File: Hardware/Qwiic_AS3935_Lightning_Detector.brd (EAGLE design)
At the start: 25.4 x 25.4 mm, 69 parts, among them U1 AS3935

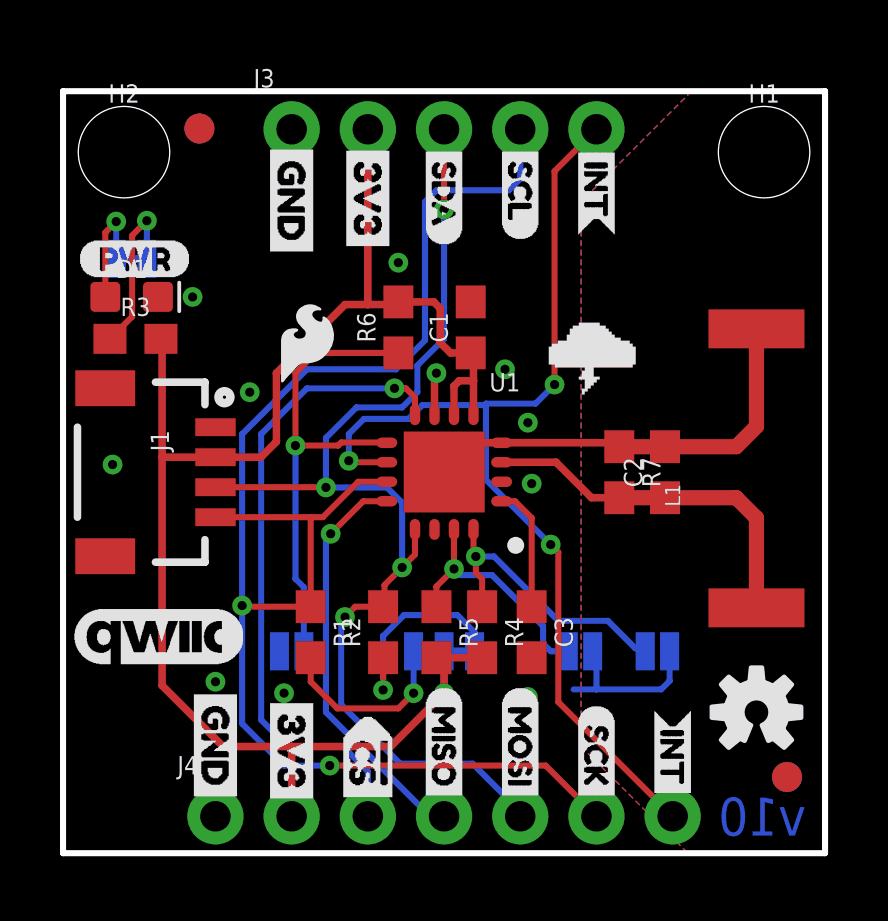
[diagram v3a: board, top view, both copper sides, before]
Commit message: Moves drill hits near standoff, moves LED jumper down, renames IRQ net to INT, and adds info on other address options
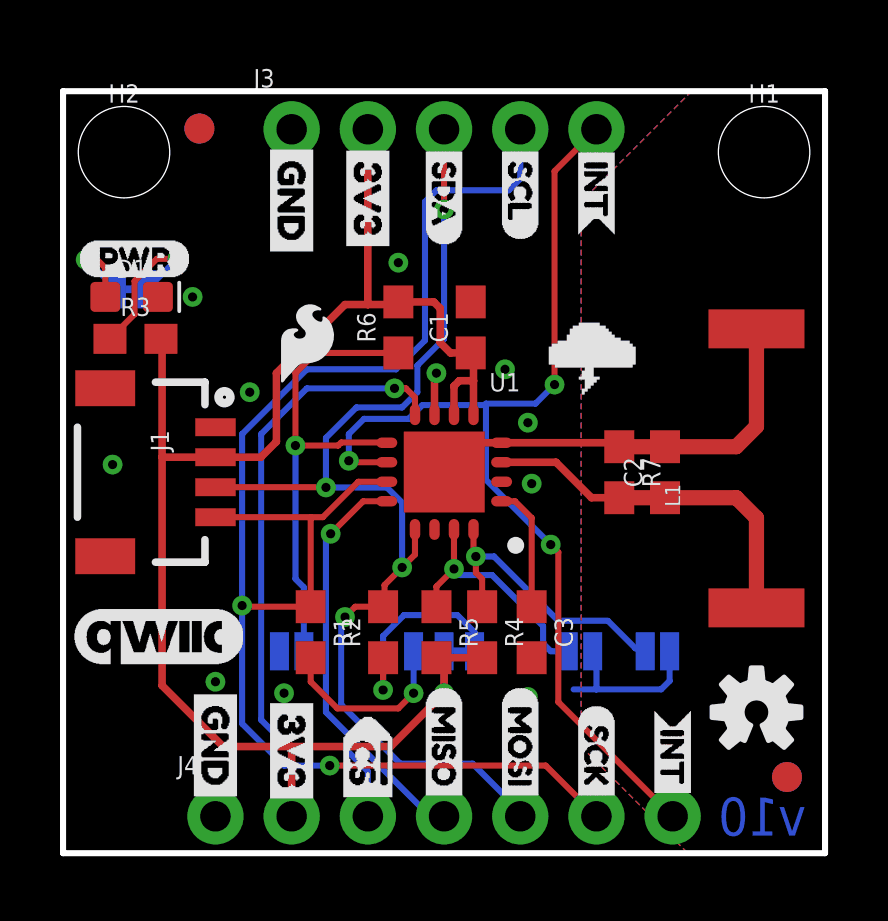
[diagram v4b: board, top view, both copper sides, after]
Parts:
- moved JP5 1.02 mm to (2.29, 18.8)
- moved U$1 1.02 mm to (4.00, 17.0)
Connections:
- net IRQ renamed INT
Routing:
- net N$5: track 3.91 -> 3.17 mm
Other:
- board text added: "Units in Inches"
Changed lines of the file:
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@@
 <setting verticaltext="up"/>
 </settings>
-<grid distance="0.01" unitdist="inch" unit="inch" style="lines" multiple="1" display="yes" altdistance="0.0001" altunitdist="inch" altunit="inch"/>
+<grid distance="0.01" unitdist="inch" unit="inch" style="lines" multiple="1" display="yes" altdistance="0.001" altunitdist="inch" altunit="inch"/>
 <layers>
 <layer number="1" name="Top" color="4" fill="1" visible="yes" active="yes"/>
@@
 <layer number="115" name="ReferenceISLANDS" color="7" fill="1" visible="no" active="no"/>
 <layer number="116" name="Patch_BOT" color="9" fill="4" visible="no" active="no"/>
-<layer number="117" name="PM_Ref" color="26" fill="1" visible="no" active="yes"/>
+<layer number="117" name="PM_Ref" color="26" fill="1" visible="yes" active="yes"/>
 <layer number="118" name="Rect_Pads" color="7" fill="1" visible="no" active="no"/>
-<layer number="119" name="PF_Ref" color="31" fill="1" visible="no" active="yes"/>
-<layer number="120" name="WFL_Ref" color="25" fill="1" visible="no" active="yes"/>
+<layer number="119" name="PF_Ref" color="31" fill="1" visible="yes" active="yes"/>
+<layer number="120" name="WFL_Ref" color="25" fill="1" visible="yes" active="yes"/>
 <layer number="121" name="_tsilk" color="7" fill="1" visible="no" active="no"/>
 <layer number="122" name="_bsilk" color="7" fill="1" visible="no" active="no"/>
@@
 <text x="19.177" y="-19.177" size="1.778" layer="51" font="vector">Elias Santistevan</text>
 <text x="24.765" y="0.5842" size="1.27" layer="16" font="vector" ratio="15" rot="MR0">v10</text>
+<dimension x1="25.4" y1="25.4" x2="0" y2="25.4" x3="12.7" y3="28.194" textsize="1.778" textratio="15" layer="47" dtype="horizontal" unit="inch"/>
+<dimension x1="25.4" y1="0" x2="25.4" y2="25.4" x3="30.226" y3="12.7" textsize="1.778" textratio="15" layer="47" dtype="horizontal" unit="inch"/>
+<text x="4.318" y="-4.572" size="1.778" layer="47" font="vector" ratio="15">Units in Inches</text>
 </plain>
 <attributes>
@@
 <attribute name="VALUE" x="2.032" y="21.717" size="0.6096" layer="27" font="vector" ratio="20" align="top-center"/>
 </element>
-<element name="JP5" library="SparkFun-Jumpers" package="SMT-JUMPER_2_NC_TRACE_SILK" value="LED" x="2.286" y="19.812" smashed="yes" rot="MR180">
-<attribute name="NAME" x="2.286" y="18.669" size="0.6096" layer="26" font="vector" ratio="20" rot="MR180" align="bottom-center"/>
-<attribute name="VALUE" x="2.286" y="20.955" size="0.6096" layer="28" font="vector" ratio="20" rot="MR180" align="top-center"/>
-</element>
-<element name="U$1" library="LED" package="LED0" value="" x="4.003040625" y="17.973040625" smashed="yes" rot="MR0"/>
+<element name="JP5" library="SparkFun-Jumpers" package="SMT-JUMPER_2_NC_TRACE_SILK" value="LED" x="2.286" y="18.796" smashed="yes" rot="MR180">
+<attribute name="NAME" x="2.286" y="17.653" size="0.6096" layer="26" font="vector" ratio="20" rot="MR180" align="bottom-center"/>
+<attribute name="VALUE" x="2.286" y="19.939" size="0.6096" layer="28" font="vector" ratio="20" rot="MR180" align="top-center"/>
+</element>
+<element name="U$1" library="LED" package="LED0" value="" x="4.003040625" y="16.957040625" smashed="yes" rot="MR0"/>
 </elements>
 <signals>
@@
 <wire x1="16.4324" y1="13.0316" x2="14.6186" y2="13.0316" width="0.254" layer="1"/>
 </signal>
-<signal name="IRQ">
+<signal name="INT">
 <contactref element="J4" pad="7"/>
 <contactref element="J3" pad="5"/>
@@
 <wire x1="15.748" y1="14.986" x2="16.383" y2="15.621" width="0.2032" layer="16"/>
 <contactref element="U1" pad="10"/>
-<wire x1="10.7422" y1="13.081" x2="10.7916" y2="13.0316" width="0.2032" layer="1"/>
 <wire x1="9.525" y1="13.081" x2="9.5744" y2="13.0316" width="0.2032" layer="1"/>
 <wire x1="9.5744" y1="13.0316" x2="10.7916" y2="13.0316" width="0.2032" layer="1"/>
@@
 <contactref element="R3" pad="1"/>
 <contactref element="JP5" pad="2"/>
-<wire x1="1.563" y1="17.145" x2="2.30378125" y2="17.88578125" width="0.2032" layer="1"/>
-<wire x1="2.30378125" y1="20.59178125" x2="2.794" y2="21.082" width="0.2032" layer="1"/>
-<via x="2.794" y="21.082" extent="1-16" drill="0.3048"/>
-<wire x1="2.794" y1="21.082" x2="2.794" y2="19.812" width="0.2032" layer="16"/>
-<wire x1="2.30378125" y1="17.88578125" x2="2.30378125" y2="20.59178125" width="0.2032" layer="1"/>
+<via x="3.81" y="19.812" extent="1-16" drill="0.3048"/>
+<wire x1="3.81" y1="19.812" x2="2.794" y2="18.796" width="0.2032" layer="16"/>
+<wire x1="2.3836" y1="19.0698625" x2="3.1257375" y2="19.812" width="0.2032" layer="1"/>
+<wire x1="3.1257375" y1="19.812" x2="3.81" y2="19.812" width="0.2032" layer="1"/>
+<wire x1="1.563" y1="17.145" x2="2.3836" y2="17.9656" width="0.2032" layer="1"/>
+<wire x1="2.3836" y1="17.9656" x2="2.3836" y2="19.0698625" width="0.2032" layer="1"/>
 </signal>
 <signal name="N$5">
 <contactref element="JP5" pad="1"/>
 <contactref element="D1" pad="A"/>
-<wire x1="1.409" y1="18.542" x2="1.409" y2="20.69115" width="0.2032" layer="1"/>
-<wire x1="1.409" y1="20.69115" x2="1.771784375" y2="21.053934375" width="0.2032" layer="1"/>
-<via x="1.771784375" y="21.053934375" extent="1-16" drill="0.3048"/>
-<wire x1="1.771784375" y1="21.053934375" x2="1.771784375" y2="19.818215625" width="0.2032" layer="16"/>
-<wire x1="1.771784375" y1="19.818215625" x2="1.778" y2="19.812" width="0.2032" layer="16"/>
+<wire x1="1.409" y1="18.542" x2="1.409" y2="19.51171875" width="0.2032" layer="1"/>
+<wire x1="1.409" y1="19.51171875" x2="1.136784375" y2="19.783934375" width="0.2032" layer="1"/>
+<wire x1="1.136784375" y1="19.783934375" x2="0.755784375" y2="19.783934375" width="0.2032" layer="1"/>
+<via x="0.755784375" y="19.783934375" extent="1-16" drill="0.3048"/>
+<wire x1="0.755784375" y1="19.783934375" x2="0.790065625" y2="19.783934375" width="0.2032" layer="16"/>
+<wire x1="0.790065625" y1="19.783934375" x2="1.778" y2="18.796" width="0.2032" layer="16"/>
 </signal>
 </signals>

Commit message: Updates lightning detector part to latest - window pane of paste rather than solid block
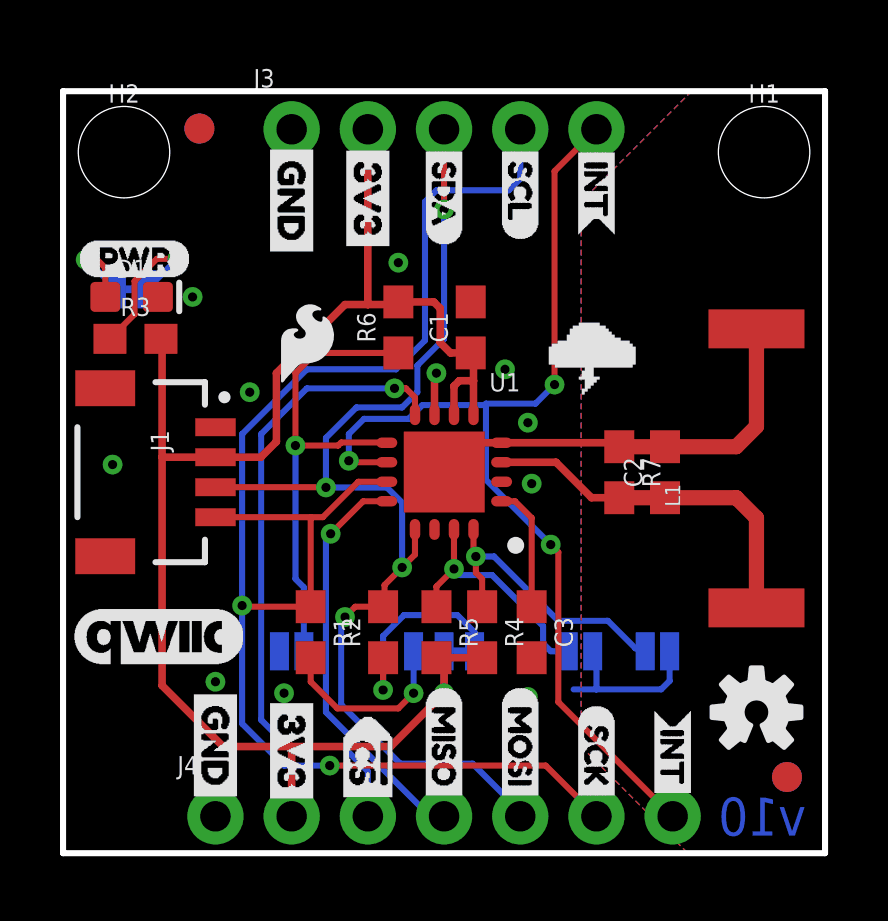
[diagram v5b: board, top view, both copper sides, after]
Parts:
- J1: device SparkFun-Connectors:1X04_1MM_RA -> SparkFun-Connectors:JST04_1MM_RA
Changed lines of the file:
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@@
 <attribute name="REV" value="" x="-7.62" y="-19.05" size="1.778" layer="27" display="off"/>
 </element>
-<element name="J1" library="SparkFun-Connectors" package="1X04_1MM_RA" value="" x="5.08" y="12.7" smashed="yes" rot="R270">
+<element name="J1" library="SparkFun-Connectors" package="JST04_1MM_RA" value="" x="5.08" y="12.7" smashed="yes" rot="R270">
 <attribute name="NAME" x="2.921" y="14.097" size="0.6096" layer="25" font="vector" ratio="20" rot="R270"/>
 <attribute name="PROD_ID" value="CONN-13694" x="5.08" y="12.7" size="1.778" layer="27" rot="R270" display="off"/>

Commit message: List of changes in description from v10 to v11
* Changes three way pull up jumper to disinclude I2C data line - also changes values to 10k
* Removes seperate I2C header and combines I2C and SPI into one header - prevents extraneous trace length on data lines
* Improves layout for better ground pour
* Moves address jumpers and SPI select jumpers
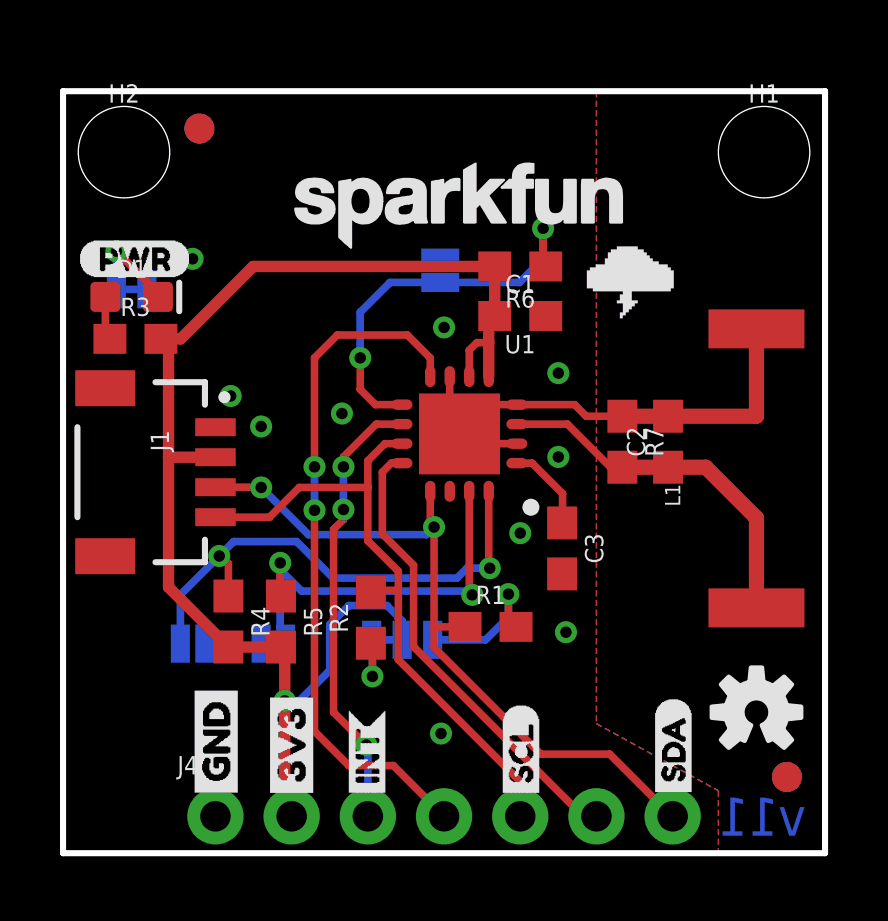
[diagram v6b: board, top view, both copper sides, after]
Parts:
- removed J3: (no value), SparkFun-Connectors:1X05_NO_SILK
- removed LOGO3: SFE_LOGO_FLAME.1_INCH, SparkFun-Aesthetics:SFE_LOGO_FLAME_.1
- removed U$11: (no value), Labels:CS#-<]-04
- removed U$13: (no value), Labels:MISO-(]-03
- removed U$15: (no value), INT_2:INT0
- removed U$16: (no value), Labels:MOSI-(]-03
- removed U$17, U$20: (no value), Labels:3V3-03
- removed U$19: (no value), Labels:SCK-(]-03
- removed U$26: (no value), SDA:SDA0
- removed U$27: (no value), SCL:SCL0
- removed U$29: (no value), INT:INT0
- removed U$38, U$9: (no value), Labels:GND-03
- removed U$4: (no value), Labels:QWIIC_COPYRIGHT_SMALL
- JP4: value JUMPER-SMT_3_2-NC_TRACE_SILK -> JUMPER-SMT_3_1-NC_TRACE_SILK; device SparkFun-Jumpers:SMT-JUMPER_3_2-NC_TRACE_SILK -> SparkFun-Jumpers:SMT-JUMPER_3_1-NC_TRACE_SILK
- R1, R2, R4, R5: value 2.2k -> 10k
- moved U$24 23.4 mm to (10.1, 1.63), turned to 90 degrees
- moved U$25 23.4 mm to (20.3, 1.68), turned to 90 degrees
- moved U$21 22.5 mm to (7.62, 1.55), turned to 90 degrees
- moved U$8 22.4 mm to (5.11, 1.60), turned to 90 degrees
- moved U$28 22.1 mm to (15.3, 1.65), turned to 90 degrees
- moved JP1 15.5 mm to (4.32, 6.99)
- moved U$36 14.4 mm to (3.81, 6.99)
- moved U$35 13.8 mm to (14.4, 21.7)
- moved JP3 13.6 mm to (12.6, 19.4), turned to 90 degrees
- moved U$33 13.0 mm to (7.87, 9.02)
- moved U$37 10.6 mm to (10.2, 6.99)
- moved JP2 10.2 mm to (7.01, 6.99), turned to 0 degrees
- moved R4 8.47 mm to (5.51, 7.72)
- moved R1 6.00 mm to (14.2, 7.54), turned to 0 degrees
- moved R5 5.19 mm to (7.26, 7.72)
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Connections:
- net !CS: now also J4.4; no longer J4.3
- net 3.3V: no longer J3.2
- net GND: now also JP5.1; no longer D1.C, J3.1
- net INT: now also J4.3; no longer J3.5, J4.7
- net MISO: now also J4.6; no longer J4.4
- net MOSI/SDA: now also J4.7, R1.1; no longer J3.3, J4.5, R2.2
- net N$1: now also D1.A; no longer JP5.2
- net N$5: now also D1.C, JP5.2; no longer D1.A, JP5.1
- net SCLK/SCL: now also J4.5, R2.2; no longer J3.4, J4.6, R1.1
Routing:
- net SCLK/SCL: track 51.4 -> 21.8 mm, vias 2 -> 0
- net INT: track 35.1 -> 15.0 mm
- net MOSI/SDA: track 38.1 -> 24.6 mm, vias 4 -> 2
- net 3.3V: track 53.8 -> 44.7 mm
- net ADD1: track 9.65 -> 17.4 mm, vias 1 -> 2
- net GND: track 22.2 -> 14.9 mm, vias 11 -> 10
- net ADD0: track 8.11 -> 14.3 mm, vias 1 -> 2
- net N$4: track 7.08 -> 2.36 mm
- net N$1: track 5.44 -> 1.46 mm, vias 1 -> 0
- net SEL_INTER: track 16.2 -> 13.3 mm, vias 1 -> 2
- net MISO: track 13.7 -> 15.5 mm, vias 1 -> 0
- net N$3: track 6.21 -> 4.80 mm
- net !CS: track 21.8 -> 23.1 mm, vias 1 -> 2
- net N$2: track 4.19 -> 2.93 mm
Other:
- board text added: "v11"
- board text removed: "v10"

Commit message: Improves silk
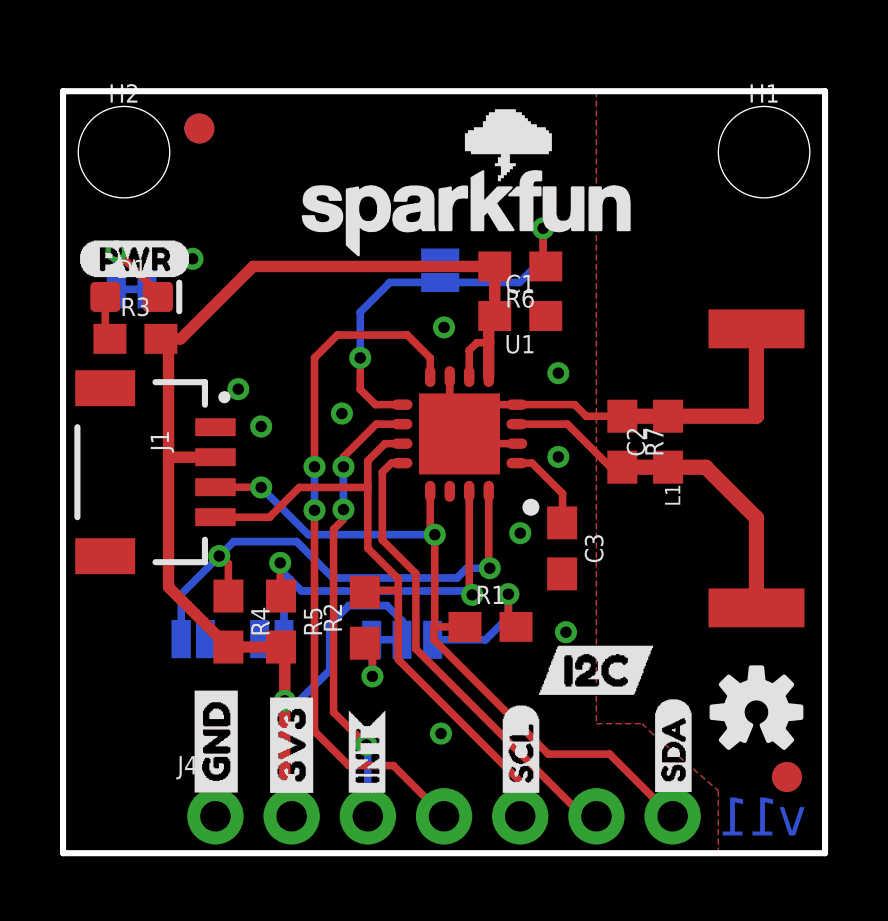
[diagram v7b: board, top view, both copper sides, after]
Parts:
- added U$2: (no value), DataLines:I2C0
- U$3: device Labels:QWIIC_COPYRIGHT_SMALL -> DataLines:SPI1
- moved U$3 18.4 mm to (19.8, 7.11), turned to 0 degrees
- moved U$14 10.2 mm to (10.2, 4.83)
- moved U$40 6.12 mm to (10.8, 23.7)
- moved U$12 5.08 mm to (17.8, 5.59)
- moved U$22 5.08 mm to (20.3, 5.59)
- moved U$23 2.54 mm to (15.2, 4.95)
- moved U$30 2.54 mm to (12.7, 4.83)
- moved U$39 1.44 mm to (18.8, 13.2)
- moved U$7 1.44 mm to (19.1, 15.2)
- moved U$6 1.27 mm to (17.9, 17.1)
- moved LOGO2 0.36 mm to (13.5, 21.3)
- moved U$35 0.25 mm to (14.6, 21.7)
- moved U$37 0.23 mm to (9.98, 7.14)
- moved U$36 0.20 mm to (3.99, 7.09)
- moved R2 0.20 mm to (10.1, 7.85)
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
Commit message: Adds "NC" silk, and updates info text in schematic for pullup resistors
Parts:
- added U$4, U$5: (no value), DataLines:NC2
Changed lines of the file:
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@@
 <element name="U$2" library="DataLines" package="I2C0" value="" x="15.748" y="6.096" smashed="yes"/>
 <element name="U$3" library="DataLines" package="SPI1" value="" x="19.812" y="7.112" smashed="yes" rot="MR0"/>
+<element name="U$4" library="DataLines" package="NC2" value="" x="12.7" y="1.524" smashed="yes" rot="R90"/>
+<element name="U$5" library="DataLines" package="NC2" value="" x="17.78" y="1.524" smashed="yes" rot="R90"/>
 </elements>
 <signals>
